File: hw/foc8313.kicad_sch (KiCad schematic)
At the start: 75 parts, among them J1 Tag Connect, J2 Encoder, J3 CAN, J4 CAN, J6 GPIO, SW1 SW_SPST, SW2 SW_SPST, U1 LMR36015SFBRNXR, U2 XC6206P332MR, U3 DRV8313PWP, U4 AS5047D, U4 STM32F103CBTx, U6 ZD24C08AE1-STGMT, X1 X322516MLB4SI

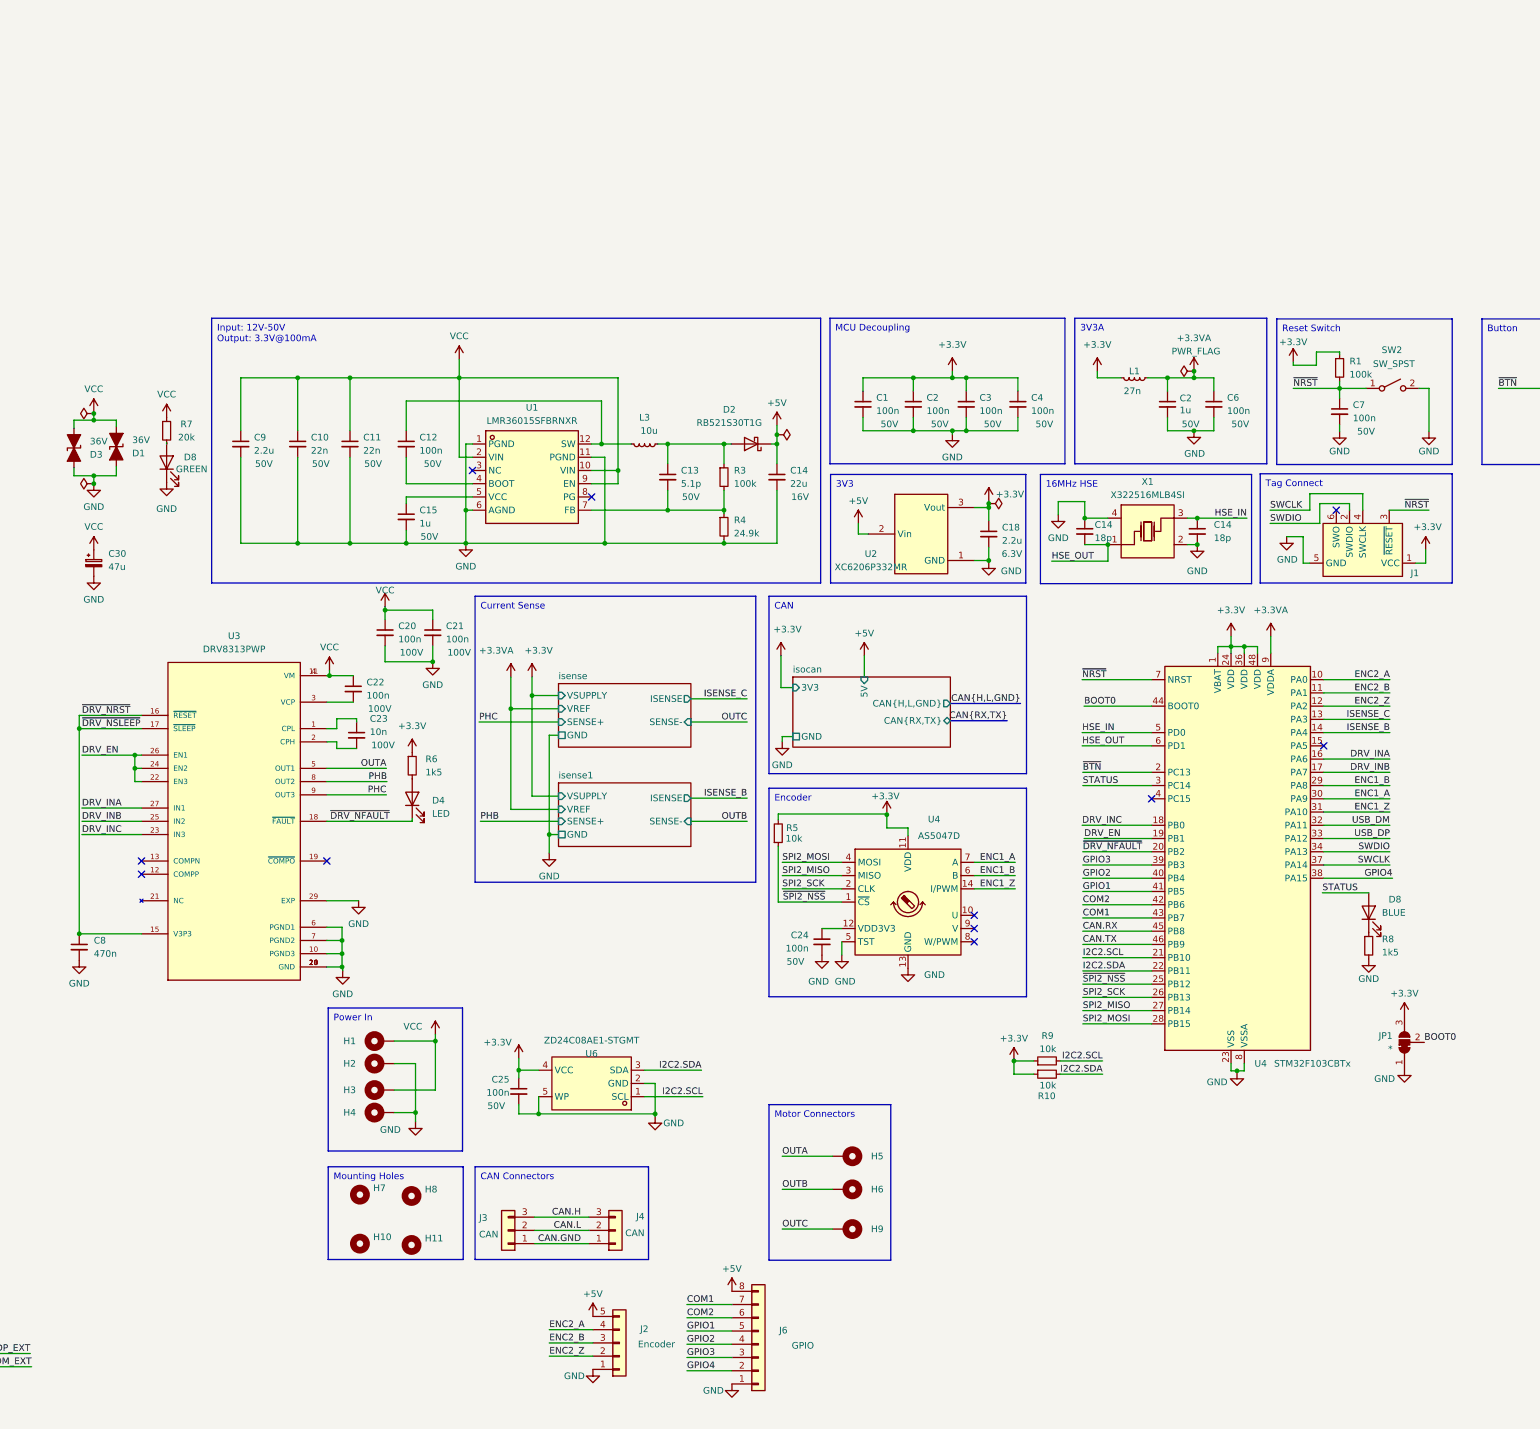
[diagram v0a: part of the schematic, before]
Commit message: [Hw] Optimised components for JLC basic parts
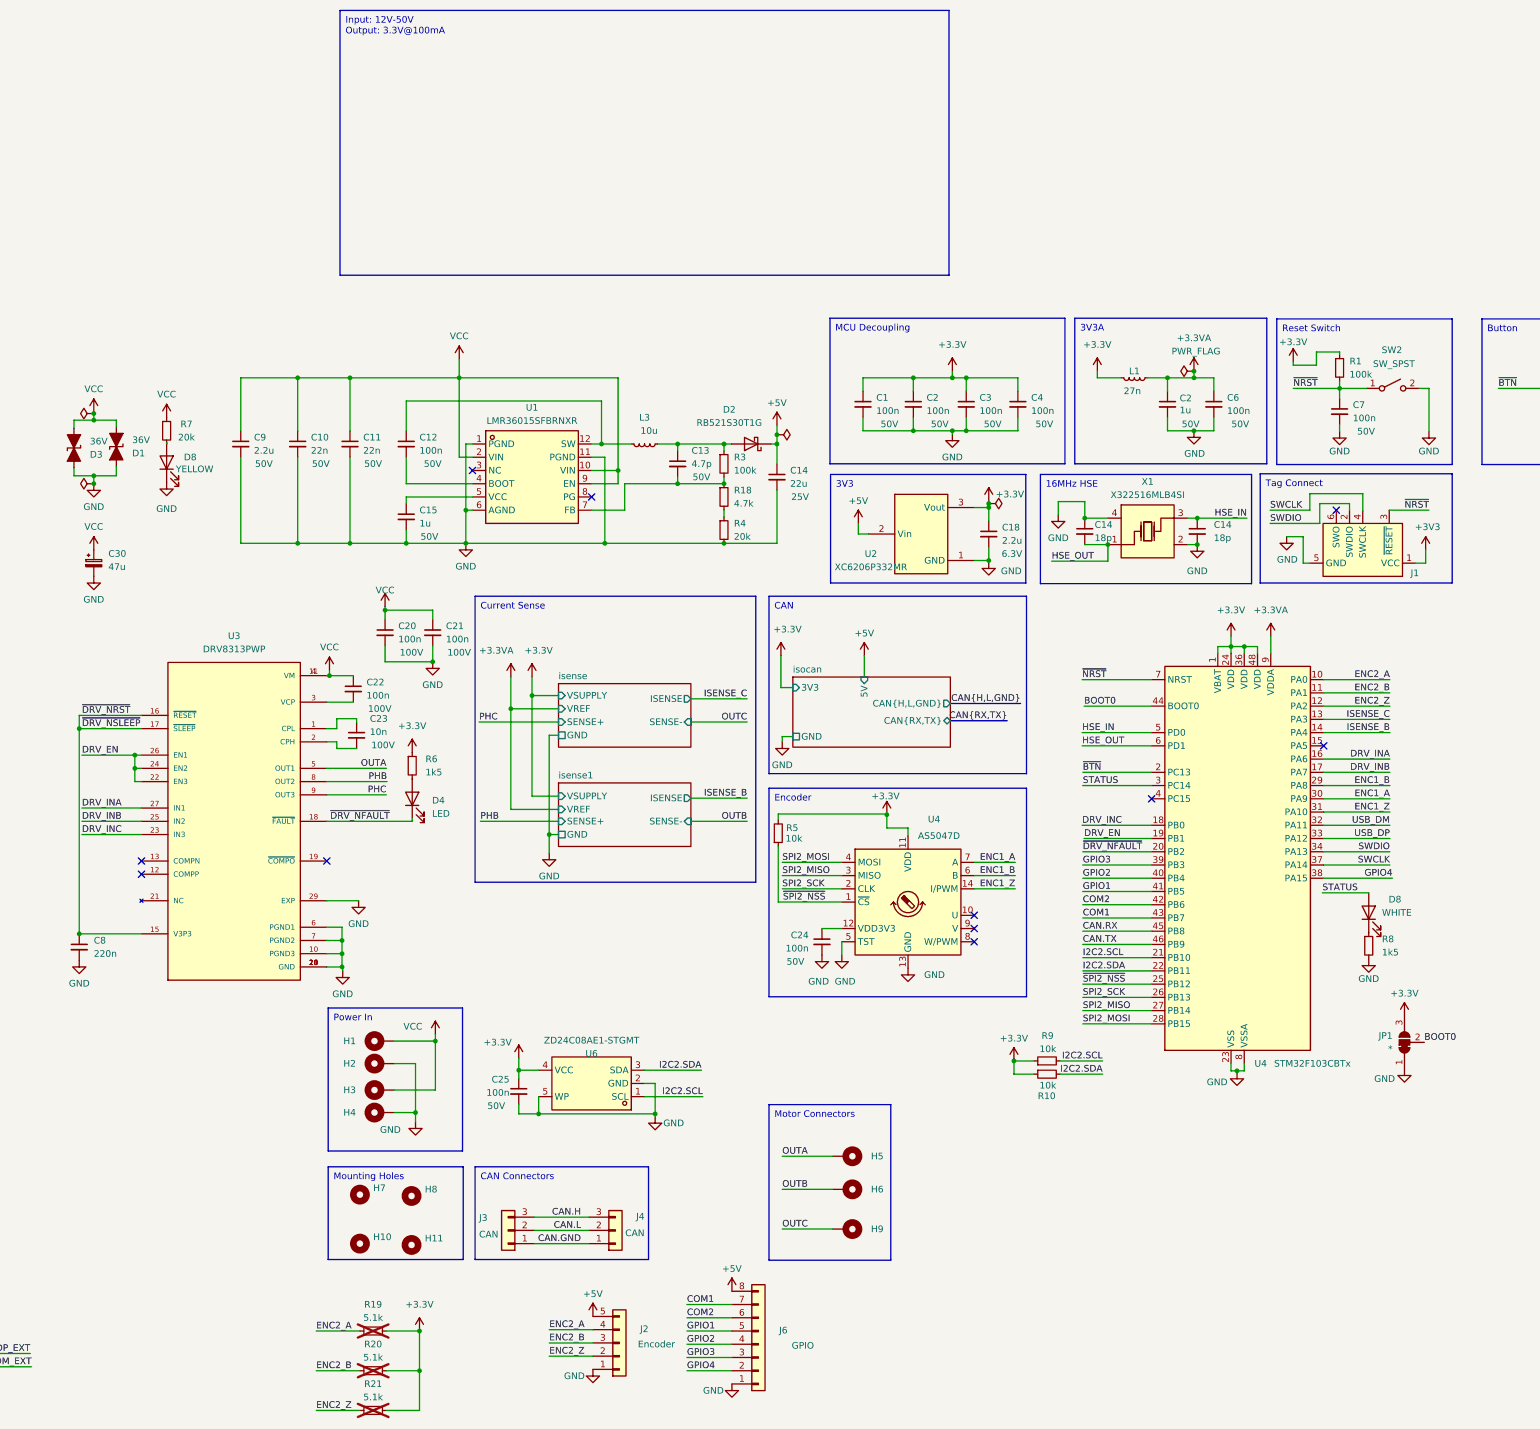
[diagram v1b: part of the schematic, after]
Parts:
- added R18: 4.7k, Resistor_SMD:R_0402_1005Metric, symbol Device:R_Small
- added R19, R20, R21: 5.1k, Resistor_SMD:R_0402_1005Metric, symbol Device:R_Small
- C13: value 5.1p -> 4.7p; LCSC C710655 -> C1567
- C14: LCSC (none) -> C1549
- C14: LCSC C98190 -> C45783; Rating 16V -> 25V
- C20, C21, C22: LCSC C162178 -> C307331
- C23: LCSC C527014 -> C15195
- C8: value 470n -> 220n; LCSC C107012 -> C16772
- D4: footprint Diode_SMD:D_0402_1005Metric -> Diode_SMD:D_0603_1608Metric; LCSC C965790 -> C2286
- D8: value BLUE -> WHITE; footprint LED_SMD:LED_0402_1005Metric -> LED_SMD:LED_0603_1608Metric; LCSC C2844007 -> C2290
- D8: value GREEN -> YELLOW; footprint LED_SMD:LED_0402_1005Metric -> LED_SMD:LED_0603_1608Metric; LCSC C434449 -> C72038
- R4: value 24.9k -> 20k; LCSC C138027 -> C25765
- SW1, SW2: LCSC (none) -> C5373430
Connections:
- net +3.3V: now also R19.2, R20.2, R21.2
- net ENC2_A: now also R19.1
- net ENC2_B: now also R20.1
- net ENC2_Z: now also R21.1
- net at C13.2, R3.2, U1.7 (FB): now also R18.1; no longer R4.1
- new net: R18.2, R4.1
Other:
- moved on the sheet: C13, R3, R4

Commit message: [Hw] Version 0.1.0 - sent for manufacture
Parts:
- added R22, R23, R24: 5.1k, Resistor_SMD:R_0402_1005Metric, symbol Device:R_Small
- H1, H10, H11, H2, H3, H4, H5, H6, H7, H8, H9: now left out of the parts list
- J3, J4: LCSC Part C189895 -> C2764182
- SW1, SW2: footprint easyeda:SW-SMD_L4.7-W3.5-P3.35-EH -> easyeda:SW-TH_PANASONIC_EVPAKE31A; LCSC C5373430 -> C569760
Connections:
- net +3.3V: now also R22.2, R23.2, R24.2
- net ENC1_A: now also R22.1
- net ENC1_B: now also R23.1
- net ENC1_Z: now also R24.1

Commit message: [Hw] WIP begun revisions for v0.2.0
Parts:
- removed D2: RB521S30T1G, Diode_SMD:D_SOD-523, symbol Device:D_Schottky
- added R25: 100k, Resistor_SMD:R_0402_1005Metric, symbol Device:R_Small
- added R26: 10k, Resistor_SMD:R_0402_1005Metric, symbol Device:R_Small
- C13: value 4.7p -> 100n; LCSC C1567 -> C307331
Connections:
- net +3V3 is gone; now on net +3.3V: J1.1 (VCC)
- net +3.3V: now also U2.2 (Vout); no longer U2.3 (Vout)
- net +5V: now also L3.1, R3.1, U2.3 (Vin); no longer U2.2 (Vin)
- net +5VD: now also USB1.A4 (VBUS), USB1.A9 (VBUS), USB1.B4 (VBUS), USB1.B9 (VBUS); no longer USB1.A12 (VBUS), USB1.A7 (VBUS), USB1.B1 (VBUS), USB1.B6 (VBUS)
- net GND: now also C13.2, USB1.A12 (GND), USB1.B1 (GND), USB1.B12 (GND), R26.1; no longer USB1.A4 (GND), USB1.B11 (GND), USB1.B9 (GND)
- net USB_DM_EXT: now also USB1.A7 (DN1), USB1.B7 (DN2); no longer USB1.A10 (DN1), USB1.B3 (DN2)
- net USB_DP_EXT: now also USB1.A6 (DP1), USB1.B6 (DP2); no longer USB1.A9 (DP1), USB1.B4 (DP2)
- net VCC: now also R25.1
- net VSENSE: now reaches U4.15 (PA5)
- net VSENSE: now also C13.1, R25.2, R26.2
- net at R18.1, R3.2, U1.7 (FB): no longer C13.2
- net at R14.1: now also USB1.A5 (CC1); no longer USB1.A8 (CC1)
- net at C12.1, L3.2, U1.12 (SW): now also U1.3 (NC)
- no-connect marks 21 -> 19
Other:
- moved on the sheet: D8, JP1, R8, U4

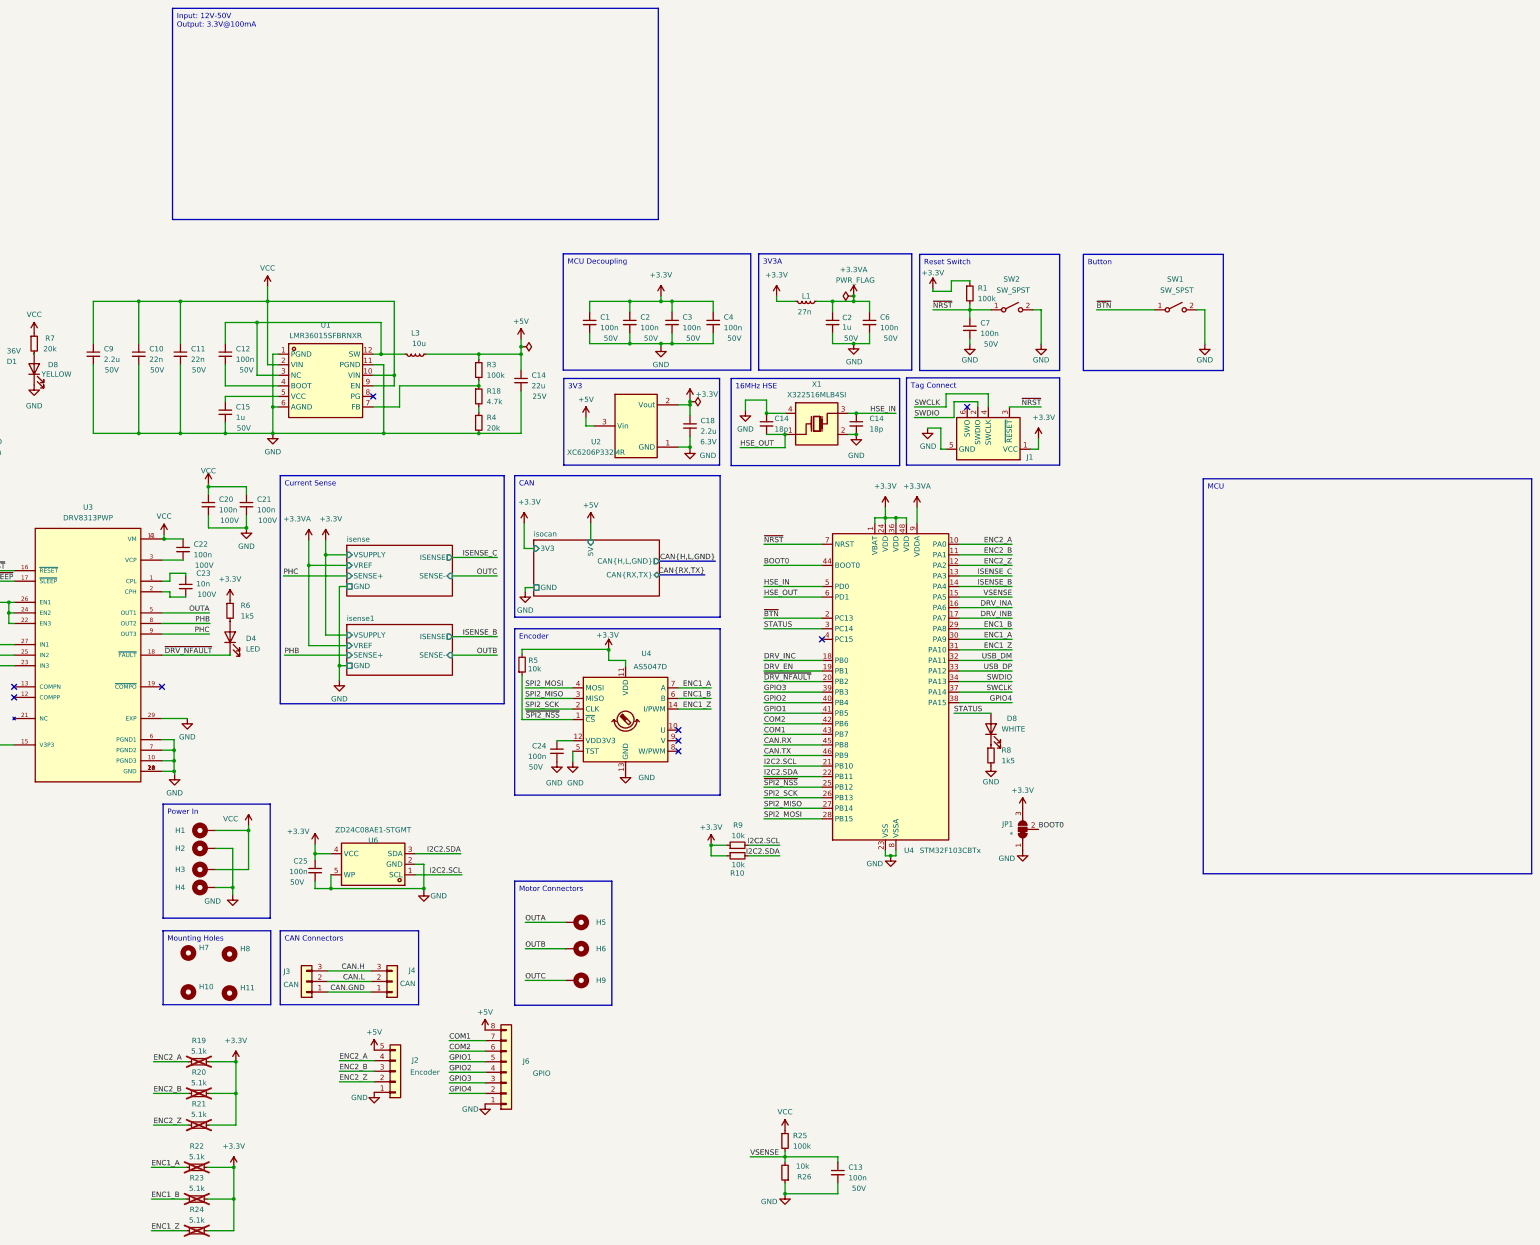
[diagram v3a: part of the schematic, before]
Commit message: [Hw] Unpinched Vcc to 3.4mm width
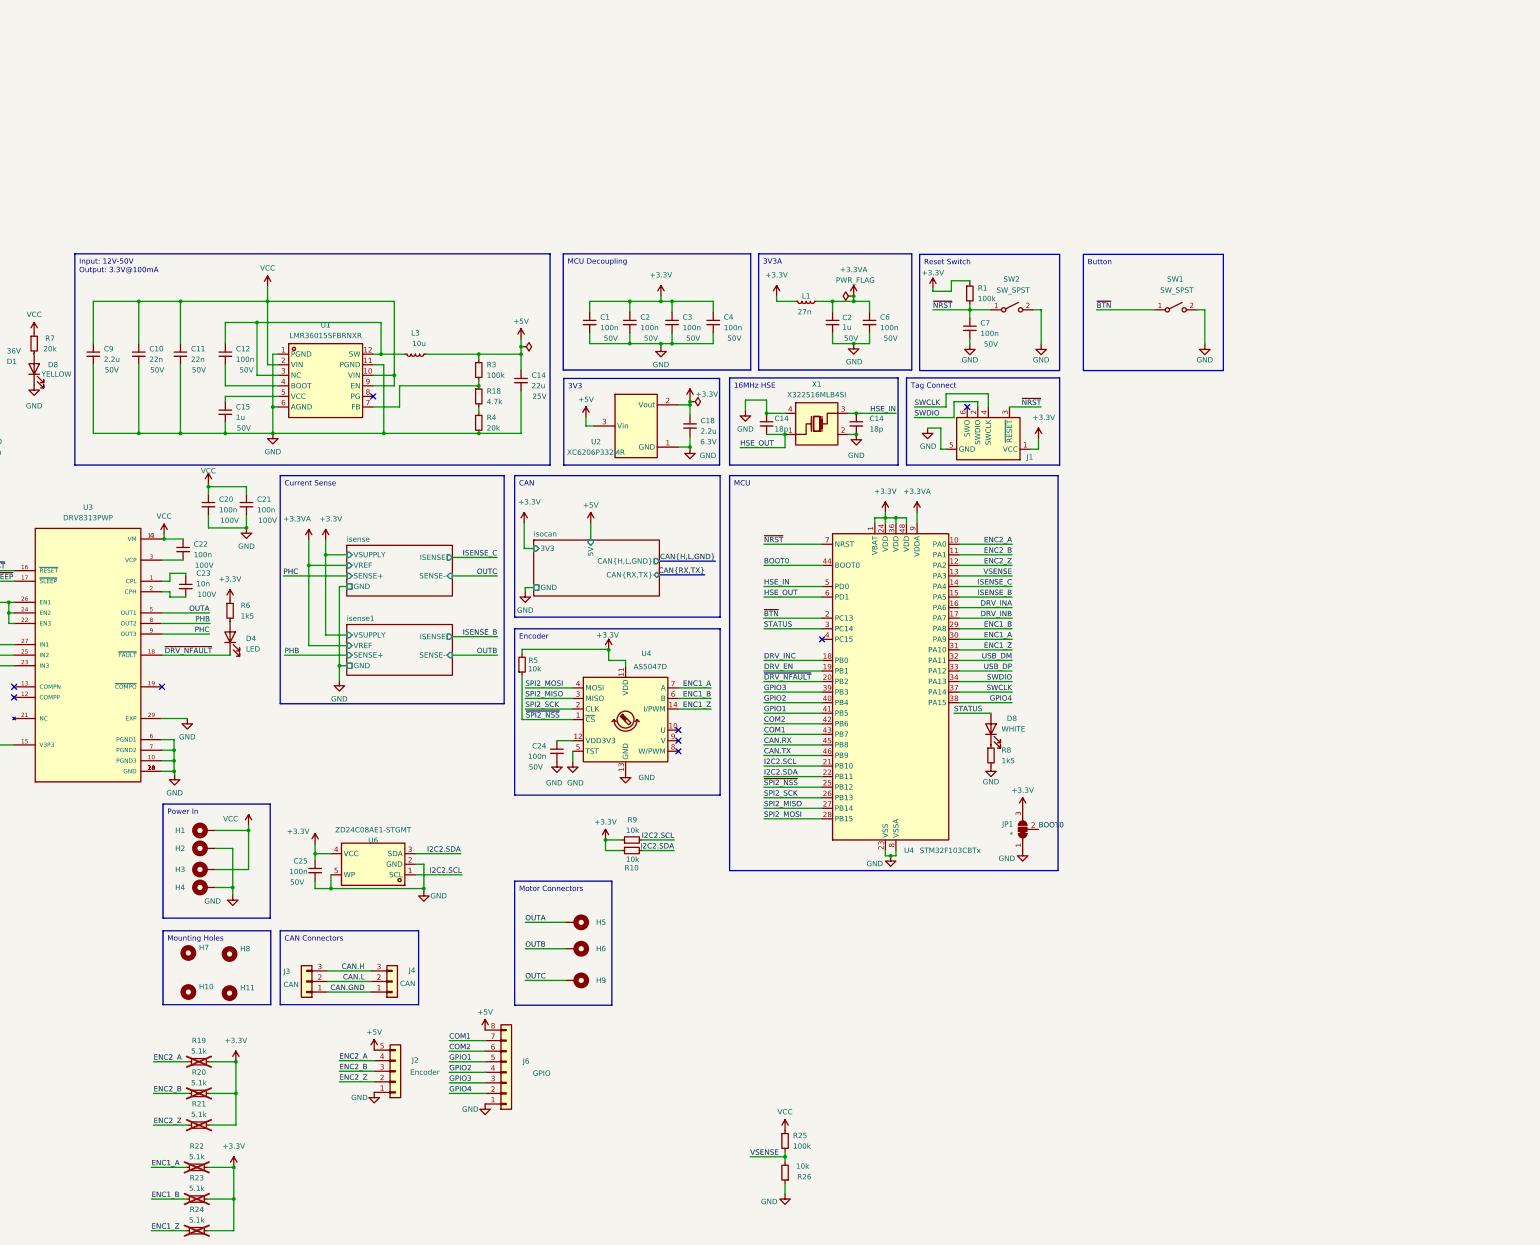
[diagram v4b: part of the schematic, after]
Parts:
- removed C13: 100n, Capacitor_SMD:C_0402_1005Metric, symbol Device:C_Small
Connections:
- net ISENSE_B: now also U4.15 (PA5); no longer U4.14 (PA4)
- net ISENSE_C: now also U4.14 (PA4); no longer U4.13 (PA3)
- net VSENSE: now also U4.13 (PA3); no longer U4.15 (PA5)
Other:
- moved on the sheet: R10, R9

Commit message: [Hw] Using advanced timer for PWM generation, and general purpose for encoder input
Signed-off-by: Will Haarhoff <williamhaarhoff@gmail.com>
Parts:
- removed C25: 100n, Capacitor_SMD:C_0402_1005Metric, symbol Device:C_Small
- removed R10, R9: 10k, Resistor_SMD:R_0402_1005Metric, symbol Device:R_Small
- removed U6: ZD24C08AE1-STGMT, easyeda:SOT-23-5_L3.0-W1.7-P0.95-LS2.8-BL, symbol easyeda:ZD24C08AE1-STGMT
- renumbered C14 to C16, C14 to C17, C2 to C5, D8 to D5, D8 to D7, L3 to L2, U4 to U5
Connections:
- net DRV_INA: now also U4.29 (PA8); no longer U4.16 (PA6)
- net DRV_INB: now also U4.30 (PA9); no longer U4.17 (PA7)
- net DRV_INC: now also U4.31 (PA10); no longer U4.18 (PB0)
- net ENC1_A: now also U4.17 (PA7); no longer U4.30 (PA9)
- net ENC1_B: now also U4.18 (PB0); no longer U4.29 (PA8)
- net ENC1_Z: now also U4.16 (PA6); no longer U4.31 (PA10)
